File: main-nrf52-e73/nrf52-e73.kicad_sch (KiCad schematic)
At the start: 19 parts, among them J4 SWD, J5 LTE_UART, J6 LTE_GND, U9 E73-2G4M08S1C

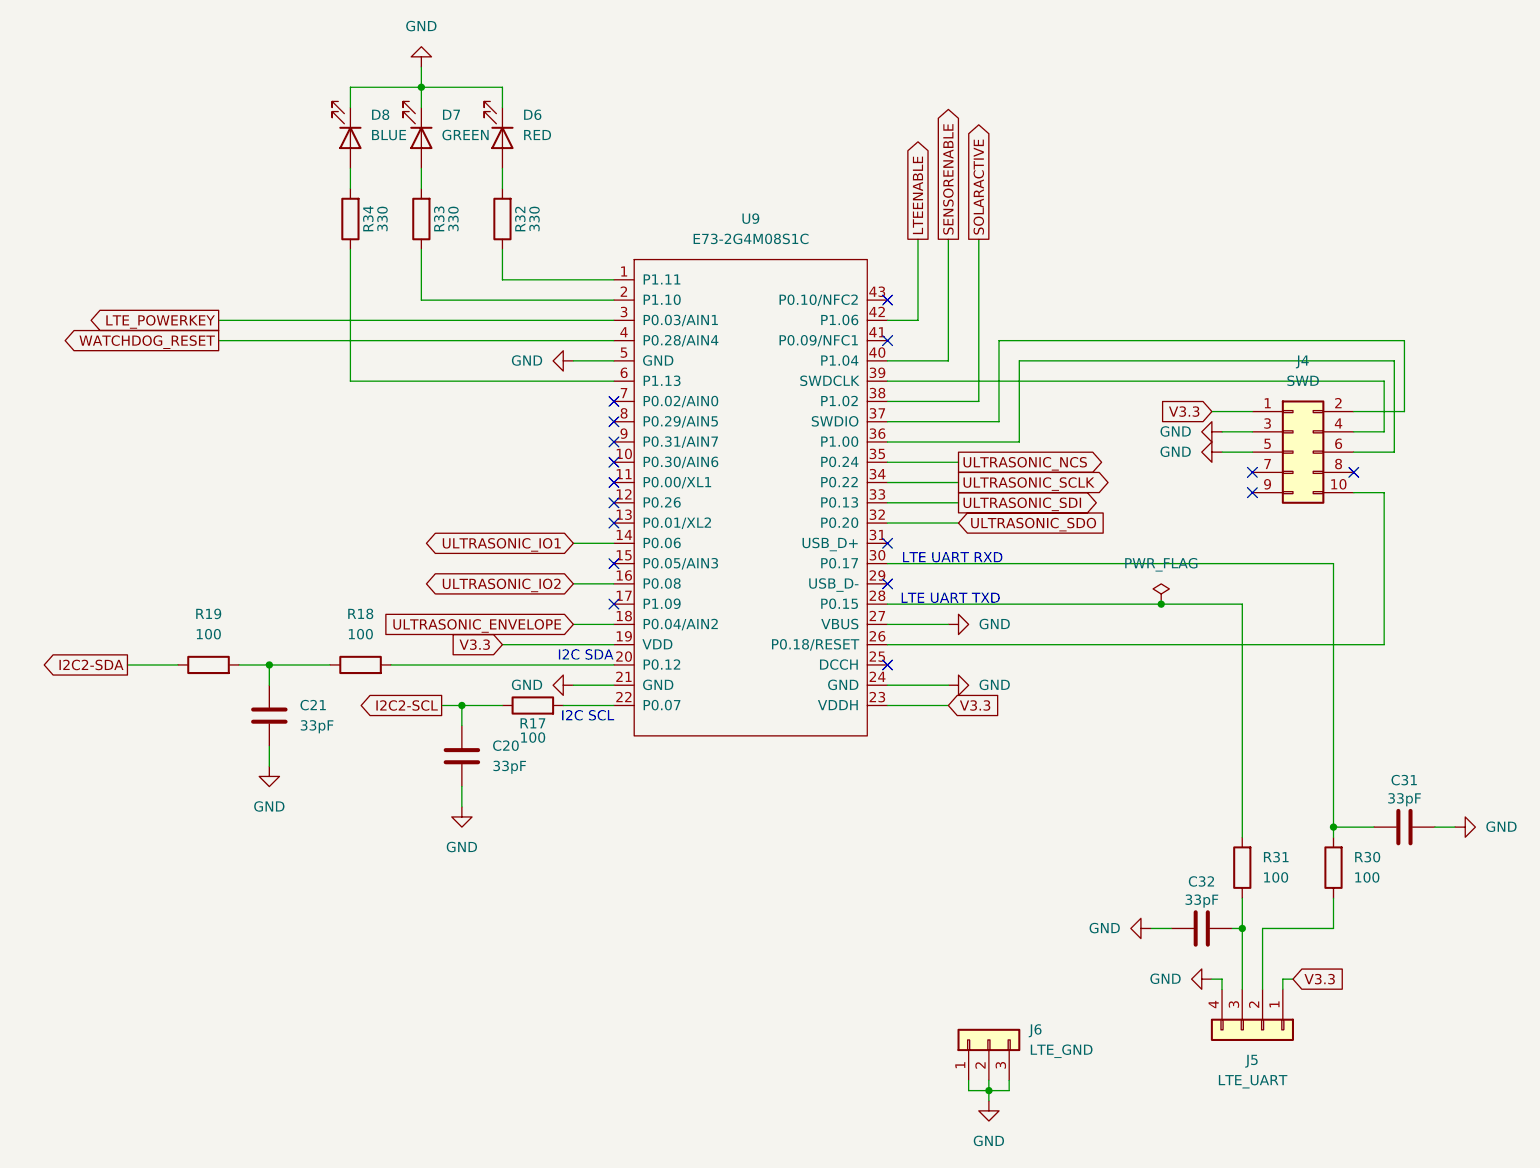
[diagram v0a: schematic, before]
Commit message: Finished first prototype of nRF52 powered main PCB.
Using Ebyte E73 module for the nRF chip.
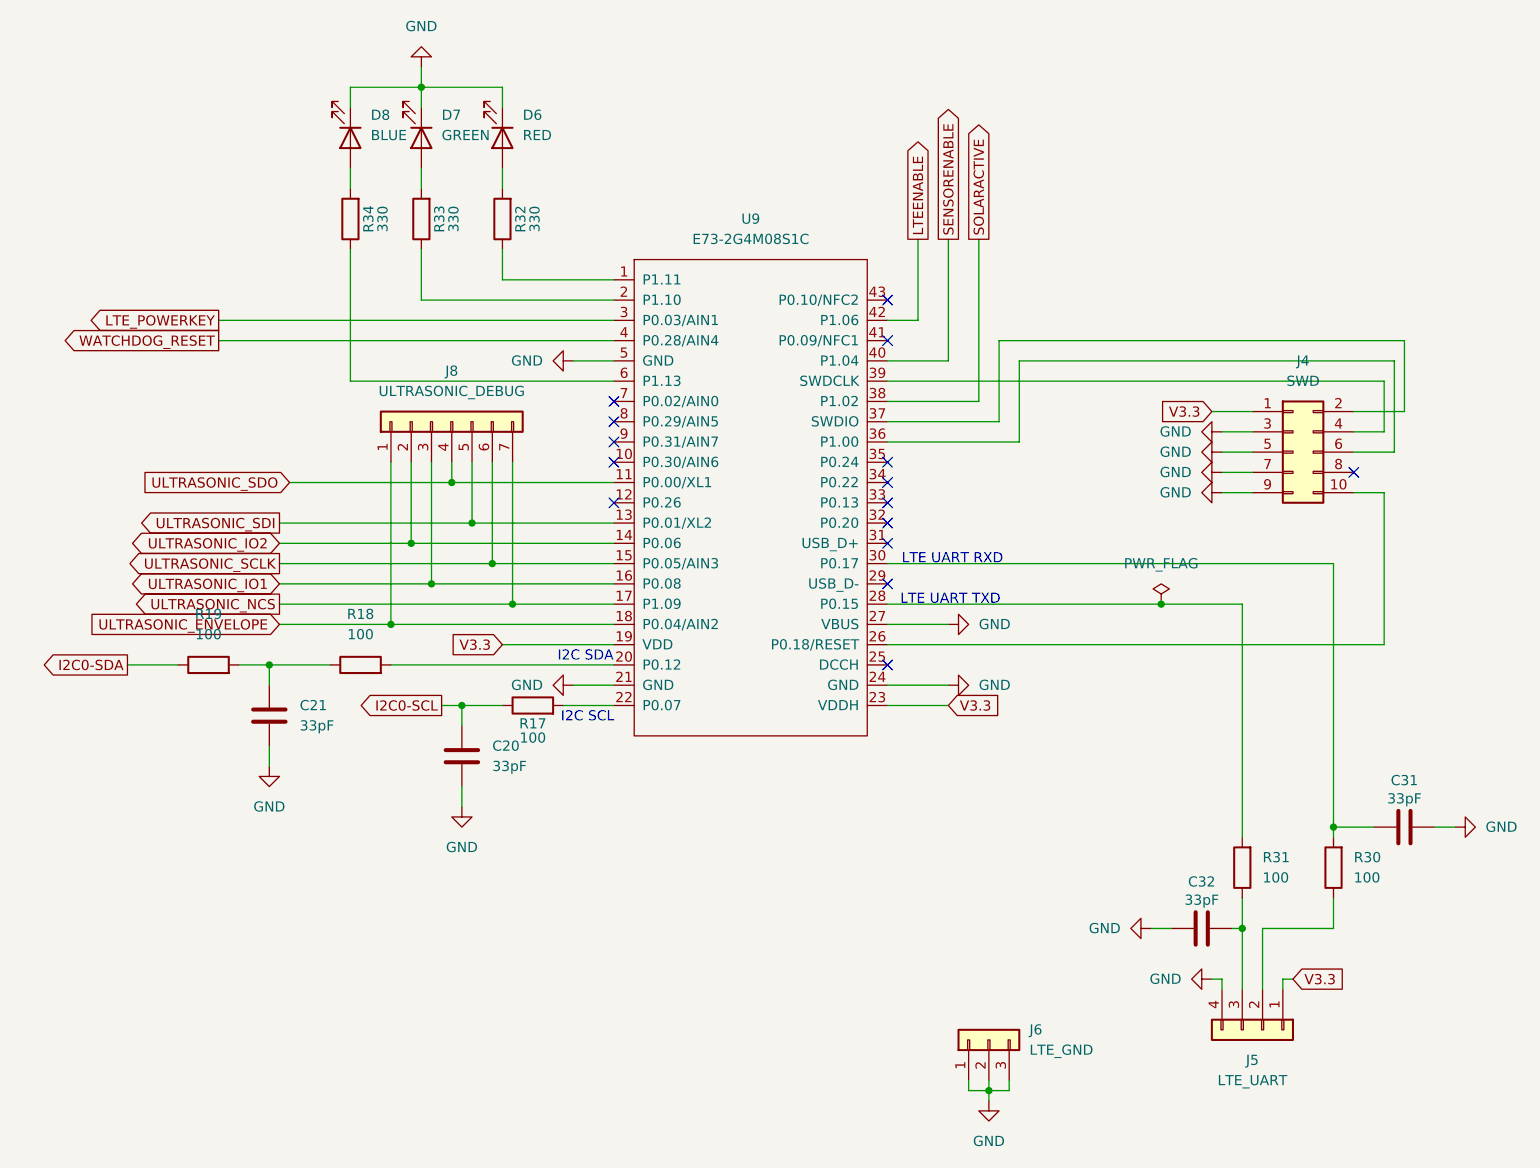
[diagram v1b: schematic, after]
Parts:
- added J8: ULTRASONIC_DEBUG, Connector_PinHeader_2.54mm:PinHeader_1x07_P2.54mm_Vertical, symbol Connector_Generic:Conn_01x07
- C20, C21: footprint Capacitor_SMD:C_0201_0603Metric -> Capacitor_SMD:C_0603_1608Metric; LCSC (none) -> C1663
- C31, C32: LCSC (none) -> C1663
- D6: LCSC (none) -> C2286
- D7: LCSC (none) -> C12624
- D8: LCSC (none) -> C2288
- J4: footprint Connector_PinSocket_1.27mm:PinSocket_2x05_P1.27mm_Vertical_SMD -> Connector_PinHeader_1.27mm:PinHeader_2x05_P1.27mm_Vertical_SMD
- R17, R18, R19, R30, R31: LCSC (none) -> C22775
- R32, R33, R34: LCSC (none) -> C23138
- U9: LCSC (none) -> C356849
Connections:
- net GND: now also J4.7 (Pin_7), J4.9 (Pin_9)
- net ULTRASONIC_ENVELOPE: now also J8.1 (Pin_1)
- net ULTRASONIC_IO1: now also U9.16 (P0.08), J8.3 (Pin_3); no longer U9.14 (P0.06)
- net ULTRASONIC_IO2: now also U9.14 (P0.06), J8.2 (Pin_2); no longer U9.16 (P0.08)
- net ULTRASONIC_NCS: now also U9.17 (P1.09), J8.7 (Pin_7); no longer U9.35 (P0.24)
- net ULTRASONIC_SCLK: now also U9.15 (P0.05/AIN3), J8.6 (Pin_6); no longer U9.34 (P0.22)
- net ULTRASONIC_SDI: now also U9.13 (P0.01/XL2), J8.5 (Pin_5); no longer U9.33 (P0.13)
- net ULTRASONIC_SDO: now also U9.11 (P0.00/XL1), J8.4 (Pin_4); no longer U9.32 (P0.20)
- net I2C2-SCL renamed I2C0-SCL
- net I2C2-SDA renamed I2C0-SDA
- no-connect marks 17 -> 15
